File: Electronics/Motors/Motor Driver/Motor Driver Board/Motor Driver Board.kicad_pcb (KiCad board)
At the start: 4 copper layers, 102 x 75 mm, 157 parts, among them IC201 TPS563202DRLR, IC202 TPS563202DRLR, IC301 TJA1057GT/3, IC302 STM32H723ZGT6, J201 JST-XH-2.50mm, J202 Pluggable_Terminal_01x02, J203 JST-XH-2.50mm, J204 JST-XH-2.50mm, J301 TC2030, J302 Pluggable_Terminal_01x03, J303 TYPE-C-31-M-12, J401 XT60PW-F, J402 XT60PW-F, J403 XT60PW-M, J404 XT60PW-F, J405 XT60-M-Vertical, J406 JST_2.5mm_1x5, J407 JST_2.5mm_1x5, J409 JST_2.5mm_1x5, Q201 DMP3028LFDE, SW301 SW_DIP_x02, T401 NVMFS4C05NT1G, T402 NVMFS4C05NT1G, T403 NVMFS4C05NT1G, T404 NVMFS4C05NT1G, T405 NVMFS4C05NT1G, T406 NVMFS4C05NT1G, T407 NVMFS4C05NT1G, T408 NVMFS4C05NT1G, T409 NVMFS4C05NT1G, T410 NVMFS4C05NT1G, T411 NVMFS4C05NT1G, T412 NVMFS4C05NT1G, U302 LSM6DS3, U303 USBLC6-4SC6-ES, U401 DRV8701ERGER, U402 DRV8701ERGER, U403 DRV8701ERGER, X301 25MHz_Clock, X302 32.768kHz_Clock

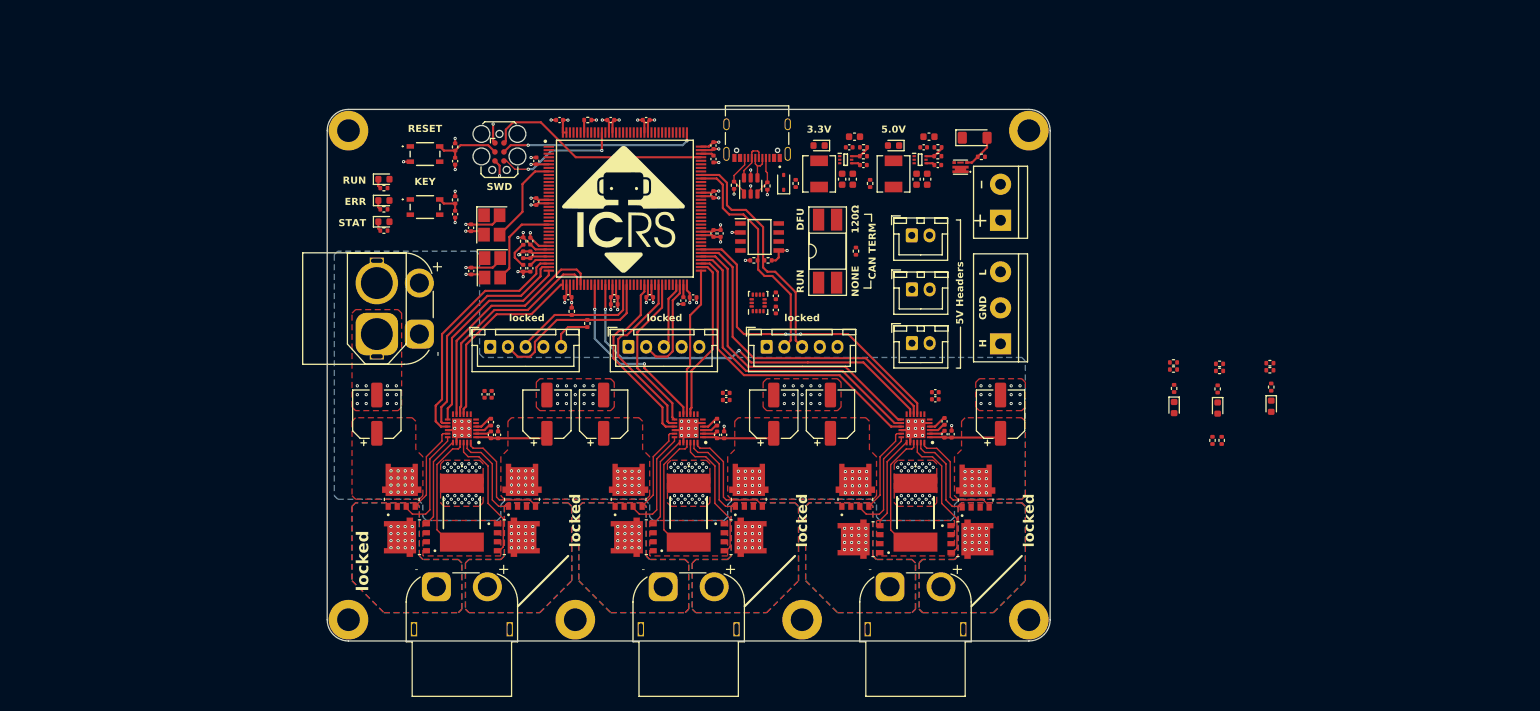
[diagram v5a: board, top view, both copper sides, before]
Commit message: Motor driver and power boards done
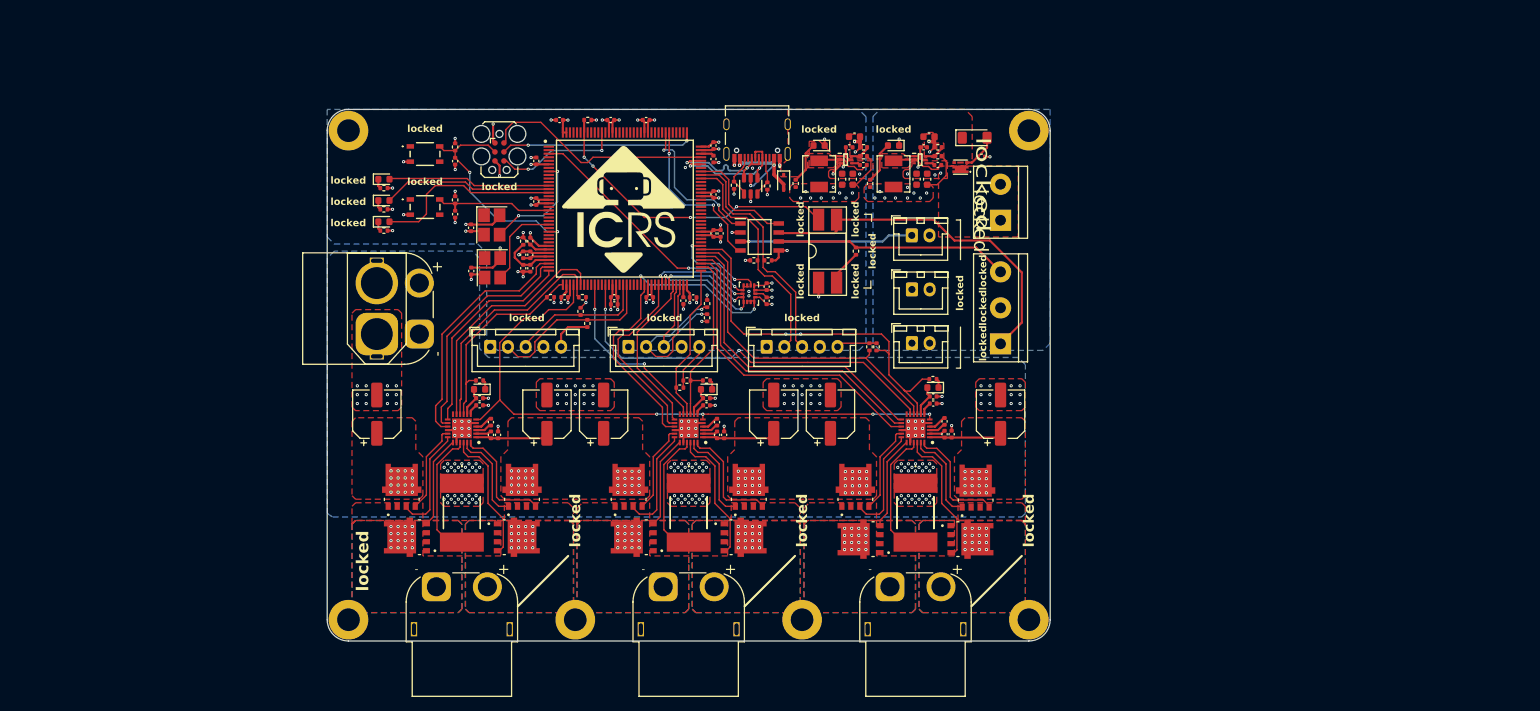
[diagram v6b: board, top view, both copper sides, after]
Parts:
- removed the G*** at (151.0, 95.0)
- added G***: LOGO, MSL Footprints:ICRS_30mm, B.Cu at (137.5, 76.2)
- added REF**: WEEE-Logo_5.6x8mm_SilkScreen, Symbol:WEEE-Logo_5.6x8mm_SilkScreen, B.Cu at (116.5, 69.5)
- added REF**: ESD-Logo_8.9x8mm_SilkScreen, Symbol:ESD-Logo_8.9x8mm_SilkScreen, B.Cu at (106.8, 69.5)
- moved D402 98.0 mm to (121.5, 99.5), turned to 180 degrees
- moved R402 98.0 mm to (121.5, 98.2), turned to 0 degrees
- moved R404 88.5 mm to (131.5, 86.5)
- moved R406 83.9 mm to (136.0, 86.5)
- moved R411 76.2 mm to (149.7, 99.3)
- moved R410 75.2 mm to (150.7, 98.3), turned to 0 degrees
- moved R316 75.1 mm to (153.6, 87.4), turned to -90 degrees
- moved R315 73.4 mm to (153.6, 89.4)
- moved D403 72.2 mm to (153.5, 99.5), turned to 180 degrees
- moved R409 72.1 mm to (153.5, 98.2), turned to 0 degrees
- moved R405 56.5 mm to (176.5, 93.5), turned to -90 degrees
- moved R403 55.6 mm to (177.5, 93.5), turned to -90 degrees
- moved D401 47.8 mm to (185.5, 99.2), turned to 180 degrees
- moved R401 47.7 mm to (185.5, 98.1), turned to 0 degrees
- moved C413 2.88 mm to (153.5, 101.8)
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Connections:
- IC302 pad 101: unconnected-(IC302-PA9-Pad101) -> SILENT
- IC302 pad 12: unconnected-(IC302-PF2-Pad12) -> LEDG
- IC302 pad 13: unconnected-(IC302-PF3-Pad13) -> LEDR
- IC302 pad 14: unconnected-(IC302-PF4-Pad14) -> LEDB
- IC302 pad 19: unconnected-(IC302-PF7-Pad19) -> BTN
- IC302 pad 3: unconnected-(IC302-PE4-Pad3) -> CS
- IC302 pad 59: unconnected-(IC302-PE8-Pad59) -> IMU_INT1
- IC302 pad 65: M2_NSLEEP -> SCK
- IC302 pad 66: unconnected-(IC302-PE13-Pad66) -> MISO
- IC302 pad 67: unconnected-(IC302-PE14-Pad67) -> MOSI
- IC302 pad 68: unconnected-(IC302-PE15-Pad68) -> M2_NSLEEP
- IC302 pad 80: unconnected-(IC302-PD11-Pad80) -> IMU_INT2
- J303 pad S2: unconnected-(J303-SHIELD-PadS1) -> unconnected-(J303-SHIELD-PadS2)
- J303 pad S3: unconnected-(J303-SHIELD-PadS1) -> unconnected-(J303-SHIELD-PadS3)
- J303 pad S4: unconnected-(J303-SHIELD-PadS1) -> unconnected-(J303-SHIELD-PadS4)
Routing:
- net VREF: track 0.00 -> 90.8 mm, vias 0 -> 4
- net /Microcontroller/CANH: track 0.00 -> 50.5 mm
- net BOOT0: track 1.76 -> 43.2 mm, vias 0 -> 4
- net CS: track 0.00 -> 35.3 mm, vias 0 -> 2
- net /Microcontroller/CANL: track 0.00 -> 33.1 mm
- net +5V: track 0.00 -> 30.8 mm, vias 0 -> 10
- net +3.3V: track 65.0 -> 94.4 mm, vias 21 -> 37
- net GND: track 75.3 -> 104.1 mm, vias 209 -> 241
- net LEDB: track 0.00 -> 26.6 mm
- net LEDR: track 0.00 -> 24.0 mm
- net CAN_RX: track 0.00 -> 23.4 mm, vias 0 -> 2
- net LEDG: track 0.00 -> 22.9 mm
- net NRST: track 9.75 -> 31.4 mm, vias 0 -> 2
- net CAN_TX: track 0.00 -> 21.1 mm, vias 0 -> 2
- net IMU_INT1: track 0.00 -> 20.6 mm, vias 0 -> 2
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- added copper zone on B.Cu, net +3.3V
- added copper zone on F.Cu, net +3.3V
- added copper zone on B.Cu, net +5V
- added copper zone on F.Cu, net +5V
- added copper zone on F.Cu, net /Power/3V3_SW
- added copper zone on F.Cu, net /Power/5V_SW
- added copper zone on F.Cu, net VIN
- added copper zone on F.Cu, net VIN_RAW
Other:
- board text removed: "+"
- board text removed: "-"
- board text removed: "120Ω"
- board text removed: "3.3V"
- board text removed: "5.0V"
- board text removed: "5V"
- board text removed: "5V Headers"
- board text removed: "CAN TERM"
- board text removed: "DFU"
- board text removed: "Designed by Ben Smith 2023"
- board text removed: "ERR"
- board text removed: "FD-CAN"
- board text removed: "GND"
- board text removed: "H"
- board text removed: "Input: 12-24V 30A"
- board text removed: "Input: 5-16V 0.5A"
- board text removed: "KEY"
- board text removed: "L"
- board text removed: "NONE"
- board text removed: "RESET"
- board text removed: "RUN"
- board text removed: "STAT"
- board text removed: "SWD"

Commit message: All boards done
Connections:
- H101 pad 1: GND -> unconnected-(H101-Pad1)
- H102 pad 1: GND -> unconnected-(H102-Pad1)
- H103 pad 1: GND -> unconnected-(H103-Pad1)
- H104 pad 1: GND -> unconnected-(H104-Pad1)
- H105 pad 1: GND -> unconnected-(H105-Pad1)
- H106 pad 1: GND -> unconnected-(H106-Pad1)
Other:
- board text added: "0"
- board text added: "1"
- board text added: "A B"
- board text added: "A PWM signal (~50kHz) on the enable pin allows speed control."
- board text added: "Brake"
- board text added: "EN"
- board text added: "Forward"
- board text added: "IMU Axis"
- board text added: "Mode"
- board text added: "PH"
- board text added: "Reverse"
- board text added: "X"
- board text added: "Y"
- board text added: "Z"
